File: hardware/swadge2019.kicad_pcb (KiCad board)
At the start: 2 copper layers, 100 x 95.3 mm, 50 parts, among them P1 PGM, P10 CONN_1, P11 CONN_1, P12 CONN_1, P13 CONN_1, P2 USBMicroB-10118192-0001LF, P3 SAO, P7 CONN_1, P8 CONN_1, P9 CONN_1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

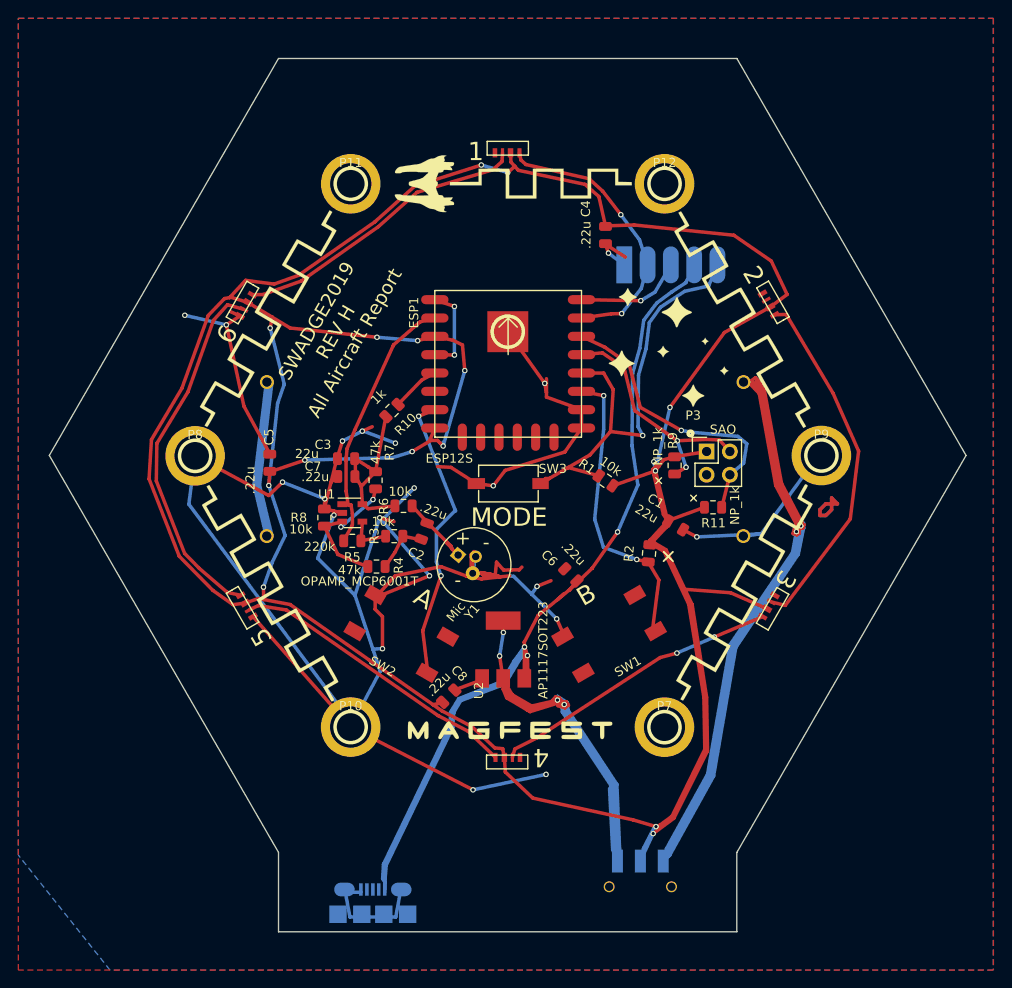
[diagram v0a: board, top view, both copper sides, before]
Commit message: Updated switch and usb models
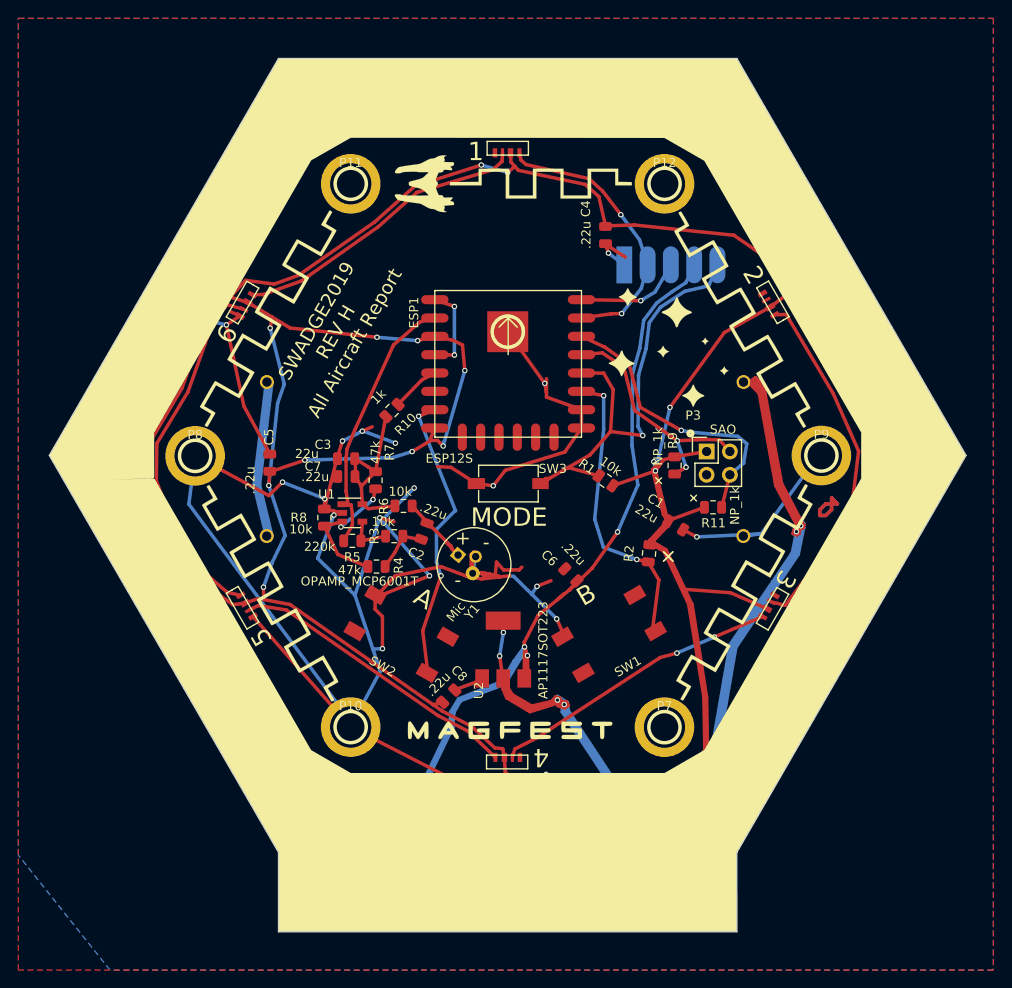
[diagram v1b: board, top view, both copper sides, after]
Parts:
- P2: value USBMicroB-10118192-0001LF -> USB_Micro-B_Molex_47346-0001; footprint USBMicroB-10118192-0001LF -> Swadge_Parts:USB_Micro-B_Molex_47346-0001
- SW7: footprint JS_SWITCH -> Swadge_Parts:SW_SPDT_PCM12
- moved SW7 3.02 mm to (91.0, 124.8)
- moved P2 0.74 mm to (61.5, 125.5)
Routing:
- net Net-(BT1-Pad1): track 185.4 -> 189.2 mm
- net Net-(SW7-Pad3): track 104.7 -> 107.8 mm
- net +3V3: track 411.2 -> 414.3 mm

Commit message: Added donut diffuser
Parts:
- added REF**: donut-diffuser, Swadge_Parts:donut-diffuser, F.Cu at (17.5, 24.4)
